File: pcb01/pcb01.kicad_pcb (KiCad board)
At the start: 2 copper layers, 7 parts, among them U1 W65C02SxP, U2 HM62256BLP, U3 27C512, U4 PAL20RS10, U5 74LS138, U6 74HCT574, U7 HM62256BLP

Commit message: more work on pcd layout
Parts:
- moved U5 100.3 mm to (13.3, 127.0)
- moved U4 92.6 mm to (41.3, 127.0)
- moved U6 86.0 mm to (108.0, 119.4), turned to -90 degrees
- moved U1 15.3 mm to (21.0, 61.0)
- moved U2 15.3 mm to (56.5, 76.2)
- moved U3 15.3 mm to (92.1, 76.2)
- moved U7 15.3 mm to (74.3, 76.2)
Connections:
- U3 pad 20: /CS_ROM -> /~{CS_ROM}
- U4 pad 16: /~{IO_SEL} -> /~{CS_RAM1}
- U4 pad 22: /~{CS_RAM1} -> /~{IO_SEL}
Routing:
- net /A14: track 28.3 -> 133.0 mm, vias 0 -> 5
- net /A12: track 42.6 -> 139.9 mm, vias 0 -> 5
- net /A13: track 58.4 -> 155.3 mm, vias 0 -> 5
- net GND: track 0.00 -> 96.4 mm
- net /A8: track 75.4 -> 154.3 mm, vias 0 -> 5
- net /A9: track 75.4 -> 154.3 mm, vias 0 -> 5
- net /A11: track 75.4 -> 151.8 mm, vias 0 -> 7
- net /~{QWE_RAM}: track 0.00 -> 70.8 mm, vias 0 -> 2
- net /SYS_CLK: track 0.00 -> 70.2 mm, vias 0 -> 1
- net /A10: track 94.3 -> 163.6 mm, vias 0 -> 7
- net /~{CS_ROM}: track 0.00 -> 65.7 mm, vias 0 -> 3
- net /R/~{W}: track 0.00 -> 62.0 mm, vias 0 -> 3
- net /A15: track 0.00 -> 61.1 mm, vias 0 -> 3
- net /~{CS_RAM0}: track 0.00 -> 50.4 mm, vias 0 -> 2
- net VCC: track 0.00 -> 46.7 mm
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- added copper zone on B.Cu, net GND
- added copper zone on F.Cu, net GND

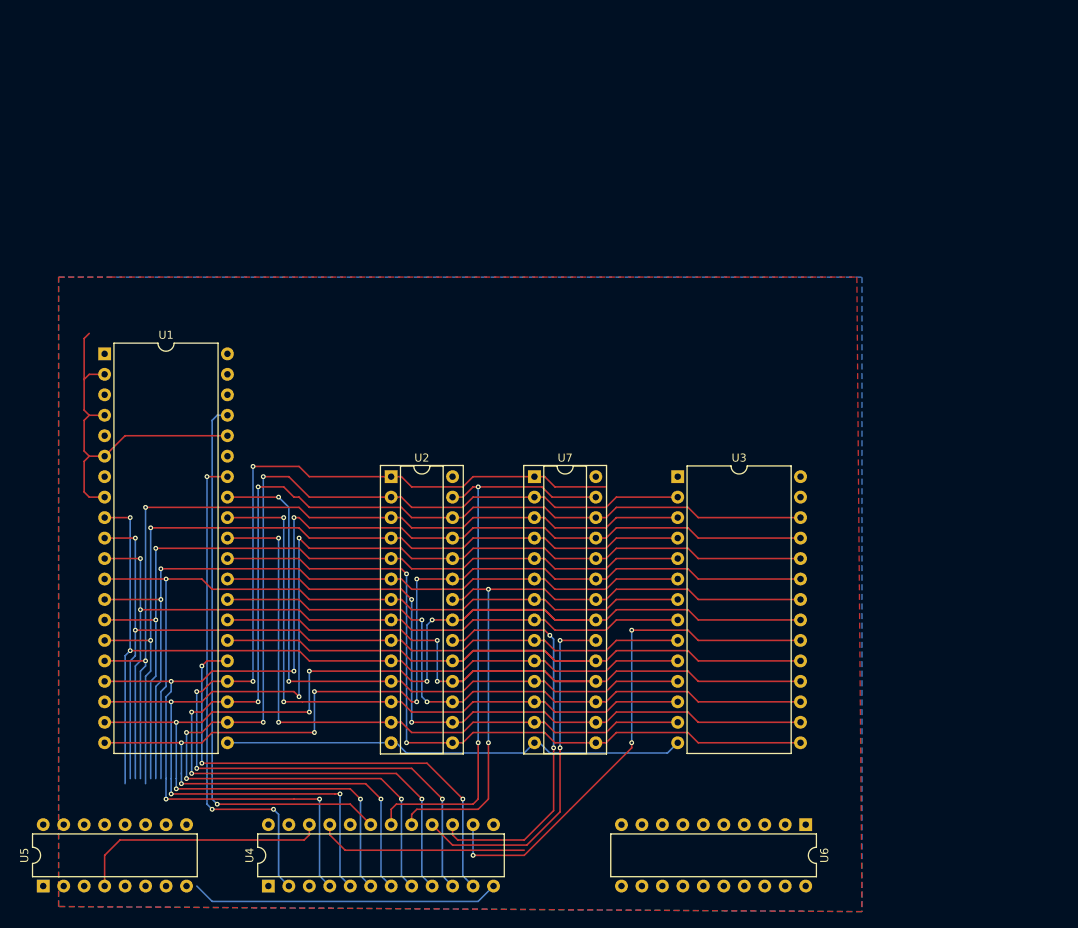
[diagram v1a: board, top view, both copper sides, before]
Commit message: wire in the R6552 uart
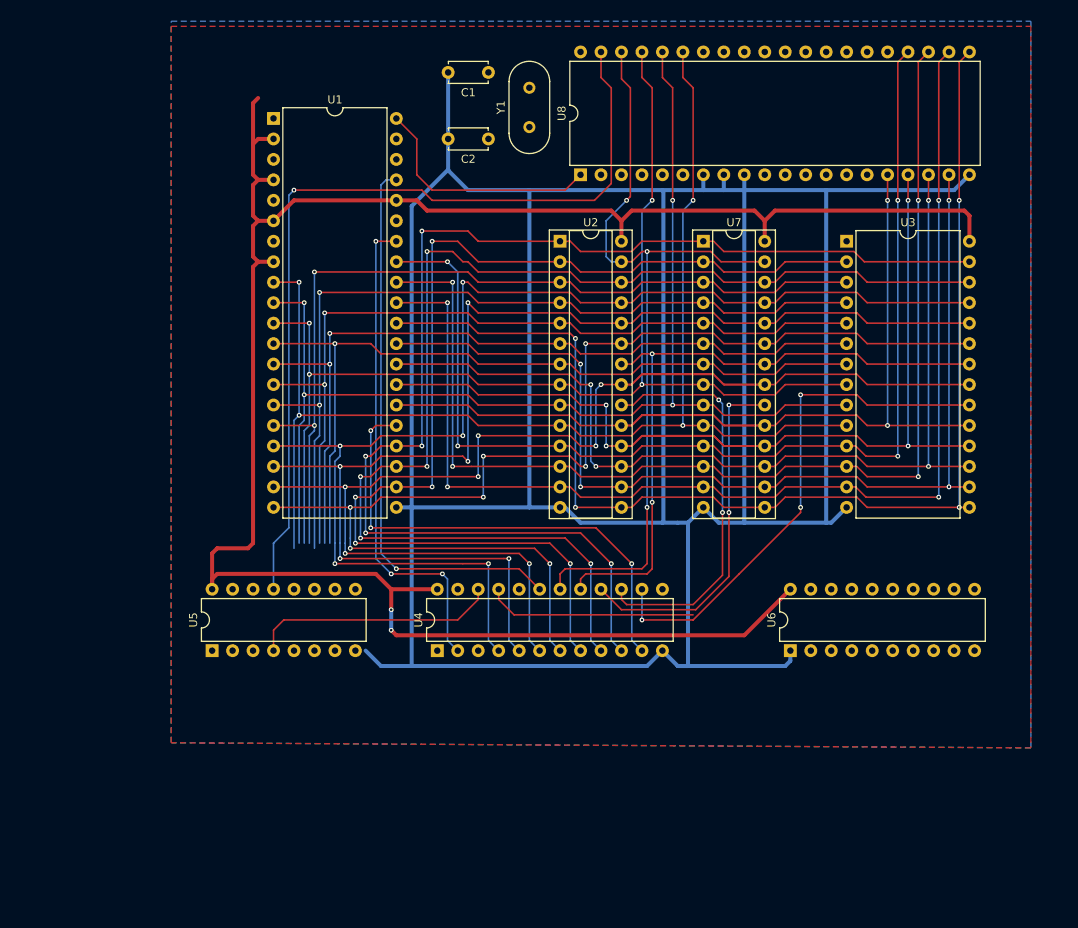
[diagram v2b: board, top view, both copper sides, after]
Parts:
- added C1: C, Capacitor_THT:C_Disc_D4.7mm_W2.5mm_P5.00mm, F.Cu at (68.6, 26.0)
- added C2: C, Capacitor_THT:C_Disc_D4.7mm_W2.5mm_P5.00mm, F.Cu at (68.6, 34.3)
- added U8: R565c52, Package_DIP:DIP-40_W15.24mm, F.Cu at (80.0, 38.7)
- added Y1: Crystal, Crystal:Crystal_HC49-4H_Vertical, F.Cu at (73.7, 32.8)
- moved U3 36.0 mm to (113.0, 47.0)
- moved U7 36.0 mm to (95.2, 47.0)
- moved U2 36.0 mm to (77.5, 47.0)
- moved U1 36.0 mm to (41.9, 31.8)
- moved U4 36.0 mm to (62.2, 97.8)
- moved U5 36.0 mm to (34.3, 97.8)
- moved U6 21.7 mm to (106.0, 97.8), turned to 90 degrees
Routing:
- net GND: track 96.4 -> 445.8 mm
- net VCC: track 46.7 -> 261.7 mm, vias 0 -> 2
- net /~{IOEN_02_UART}: track 0.00 -> 108.2 mm, vias 0 -> 1
- net /D2: track 80.8 -> 148.6 mm, vias 2 -> 4
- net /D1: track 80.8 -> 143.5 mm, vias 2 -> 4
- net /D0: track 80.1 -> 137.7 mm, vias 2 -> 4
- net /D3: track 95.0 -> 152.0 mm, vias 2 -> 4
- net /A0: track 107.0 -> 154.4 mm, vias 2 -> 4
- net /A1: track 103.9 -> 148.2 mm, vias 2 -> 4
- net /A2: track 101.3 -> 143.6 mm, vias 2 -> 4
- net /D4: track 89.5 -> 128.2 mm, vias 2 -> 4
- net /D5: track 84.1 -> 120.3 mm, vias 2 -> 4
- net /D6: track 98.2 -> 131.8 mm, vias 2 -> 4
- net /D7: track 93.1 -> 124.2 mm, vias 0 -> 2
- net /~{RES}: track 0.00 -> 29.9 mm
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- added copper zone on F.Cu, net VCC
- removed copper zone on F.Cu, net GND

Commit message: add reset circuit and filter caps
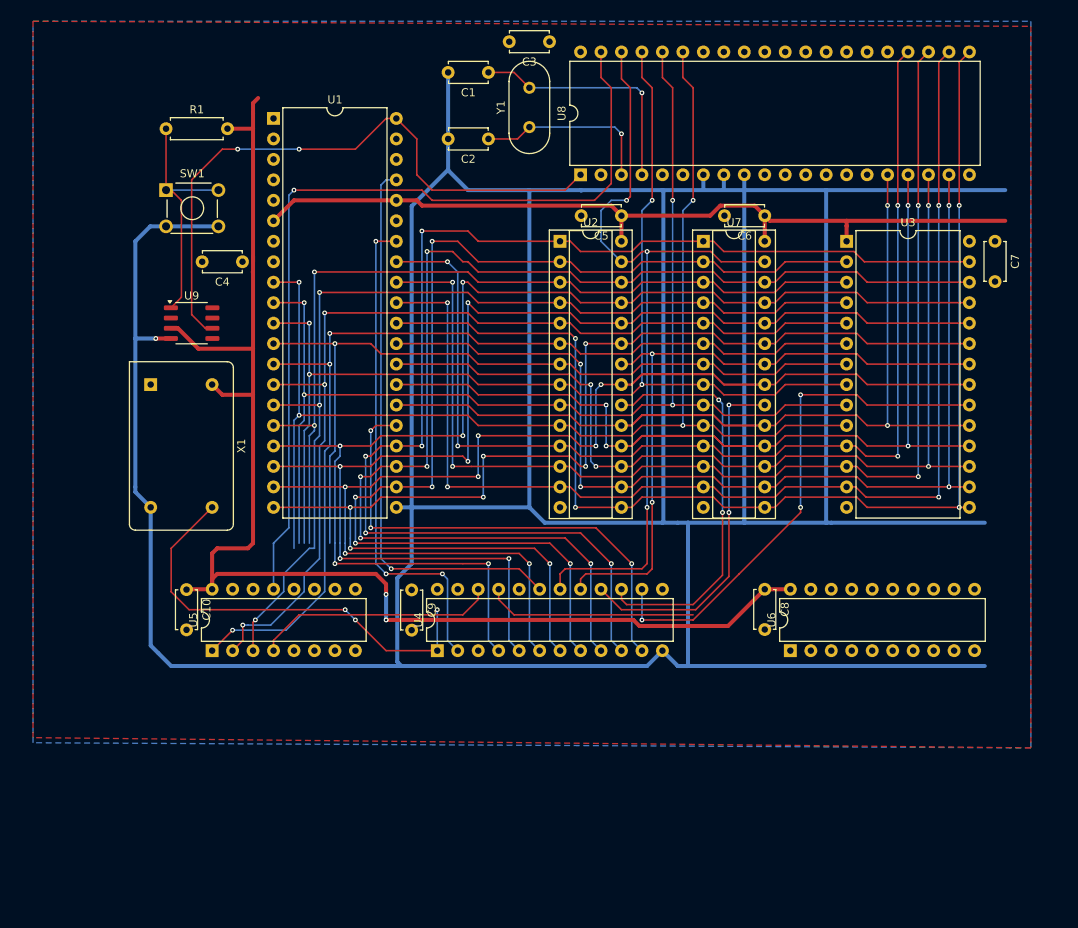
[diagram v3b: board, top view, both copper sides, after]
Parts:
- added C10: C, Capacitor_THT:C_Disc_D4.7mm_W2.5mm_P5.00mm, F.Cu at (31.1, 90.2)
- added C3: C, Capacitor_THT:C_Disc_D4.7mm_W2.5mm_P5.00mm, F.Cu at (76.2, 22.2)
- added C4: C, Capacitor_THT:C_Disc_D4.7mm_W2.5mm_P5.00mm, F.Cu at (38.1, 49.5)
- added C5: C, Capacitor_THT:C_Disc_D4.7mm_W2.5mm_P5.00mm, F.Cu at (85.1, 43.8)
- added C6: C, Capacitor_THT:C_Disc_D4.7mm_W2.5mm_P5.00mm, F.Cu at (102.9, 43.8)
- added C7: C, Capacitor_THT:C_Disc_D4.7mm_W2.5mm_P5.00mm, F.Cu at (131.4, 47.0)
- added C8: C, Capacitor_THT:C_Disc_D4.7mm_W2.5mm_P5.00mm, F.Cu at (102.9, 90.2)
- added C9: C, Capacitor_THT:C_Disc_D4.7mm_W2.5mm_P5.00mm, F.Cu at (59.1, 90.2)
- added R1: R, Resistor_THT:R_Axial_DIN0207_L6.3mm_D2.5mm_P7.62mm_Horizontal, F.Cu at (28.6, 33.0)
- added SW1: SW_Push, Button_Switch_THT:SW_TH_Tactile_Omron_B3F-10xx, F.Cu at (28.6, 40.6)
- added U9: ~, Package_SO:SO-8_3.9x4.9mm_P1.27mm, F.Cu at (31.8, 57.1)
- added X1: ACO-xxxMHz, Oscillator:Oscillator_DIP-14, F.Cu at (26.7, 64.8)
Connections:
- C1 pad 1: /UART_X1 -> /UART_X2
- C2 pad 1: /UART_X2 -> /UART_X1
- U1 pad 25: /A15 -> VCC
- U3 pad 1: /A15 -> VCC
- U4 pad 11: /A15 -> VCC
- Y1 pad 1: /UART_X2 -> /UART_X1
- Y1 pad 2: /UART_X1 -> /UART_X2
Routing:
- net GND: track 445.8 -> 581.9 mm, vias 0 -> 1
- net VCC: track 261.7 -> 333.8 mm, vias 2 -> 5
- net /A15: track 61.1 -> 0.00 mm, vias 3 -> 0
- net /CLOCK: track 0.00 -> 54.0 mm, vias 0 -> 3
- net /~{RES}: track 29.9 -> 78.5 mm, vias 0 -> 2
- net Net-(U9-~{PB_RST}): track 0.00 -> 30.4 mm
- net /UART_X2: track 0.00 -> 30.3 mm, vias 0 -> 1
- net /A4: track 100.0 -> 123.1 mm, vias 2 -> 3
- net /UART_X1: track 0.00 -> 22.5 mm, vias 0 -> 1
- net /A5: track 102.6 -> 122.4 mm, vias 2 -> 3
- net /A6: track 105.8 -> 122.0 mm, vias 2 -> 3
- net /~{QWE_RAM}: track 100.1 -> 101.0 mm
- net /~{IO_SEL}: track 30.8 -> 30.0 mm

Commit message: pcb layout should be finished...
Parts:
- added J1: DIN41612_02x32_AC, Connector_DIN:DIN41612_C_2x32_Male_Horizontal_THT, F.Cu at (123.8, 113.0)
- added J2: Conn_01x08_Socket, Connector_PinSocket_2.54mm:PinSocket_1x08_P2.54mm_Vertical, F.Cu at (108.6, 102.9)
- added J3: Conn_01x16_Socket, Connector_PinSocket_2.54mm:PinSocket_1x16_P2.54mm_Vertical, F.Cu at (49.5, 102.9)
- added J4: Conn_01x16_Socket, Connector_PinSocket_2.54mm:PinSocket_1x16_P2.54mm_Vertical, F.Cu at (135.9, 102.9)
- X1: footprint Oscillator:Oscillator_DIP-14 -> Package_DIP:DIP-14_W7.62mm
- turned X1 to 0 degrees
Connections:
- U1 pad 25: VCC -> /A15
- U4 pad 11: VCC -> /A15
- U5 pad 10: unconnected-(U5-O5-Pad10) -> /~{IOEN_05}
- U5 pad 11: unconnected-(U5-O4-Pad11) -> /~{IOEN_04}
- U5 pad 12: unconnected-(U5-O3-Pad12) -> /~{IOEN_03}
- U5 pad 7: unconnected-(U5-O7-Pad7) -> /~{IOEN_07}
- U5 pad 9: unconnected-(U5-O6-Pad9) -> /~{IOEN_06}
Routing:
- net /~{RES}: track 78.5 -> 222.8 mm, vias 2 -> 6
- net /~{IOEN_00_GPIO0}: track 0.00 -> 133.8 mm, vias 0 -> 3
- net /~{QWE_RAM}: track 101.0 -> 200.5 mm, vias 3 -> 7
- net /A0: track 154.4 -> 246.3 mm, vias 4 -> 6
- net /DISP_EN: track 26.2 -> 117.6 mm, vias 0 -> 2
- net /A15: track 0.00 -> 72.0 mm, vias 0 -> 3
- net /D0: track 137.7 -> 208.7 mm, vias 4 -> 6
- net /SYS_CLK: track 69.8 -> 138.2 mm, vias 1 -> 4
- net /D1: track 143.5 -> 204.6 mm, vias 4 -> 6
- net /A7: track 107.7 -> 164.4 mm, vias 2 -> 4
- net /D7: track 124.2 -> 173.1 mm, vias 2 -> 4
- net /D2: track 148.6 -> 197.2 mm, vias 4 -> 6
- net /~{QOE}: track 82.6 -> 128.9 mm, vias 2 -> 5
- net /D6: track 131.8 -> 177.7 mm, vias 4 -> 6
- net /A1: track 148.2 -> 192.6 mm
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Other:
- board outline added: 117.5 x 98.4 mm
- board text added: "JLCJLCJLCJLC"

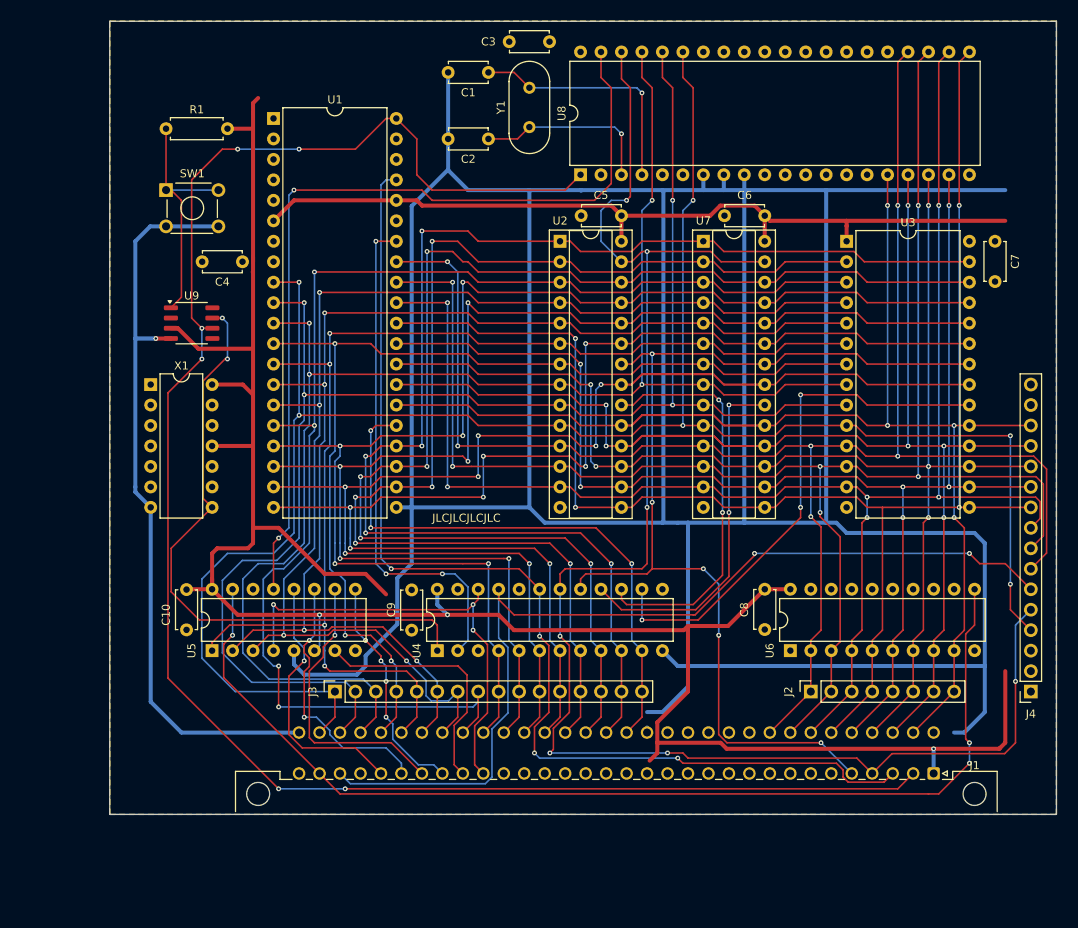
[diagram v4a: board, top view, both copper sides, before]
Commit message: fix some schematic bugs
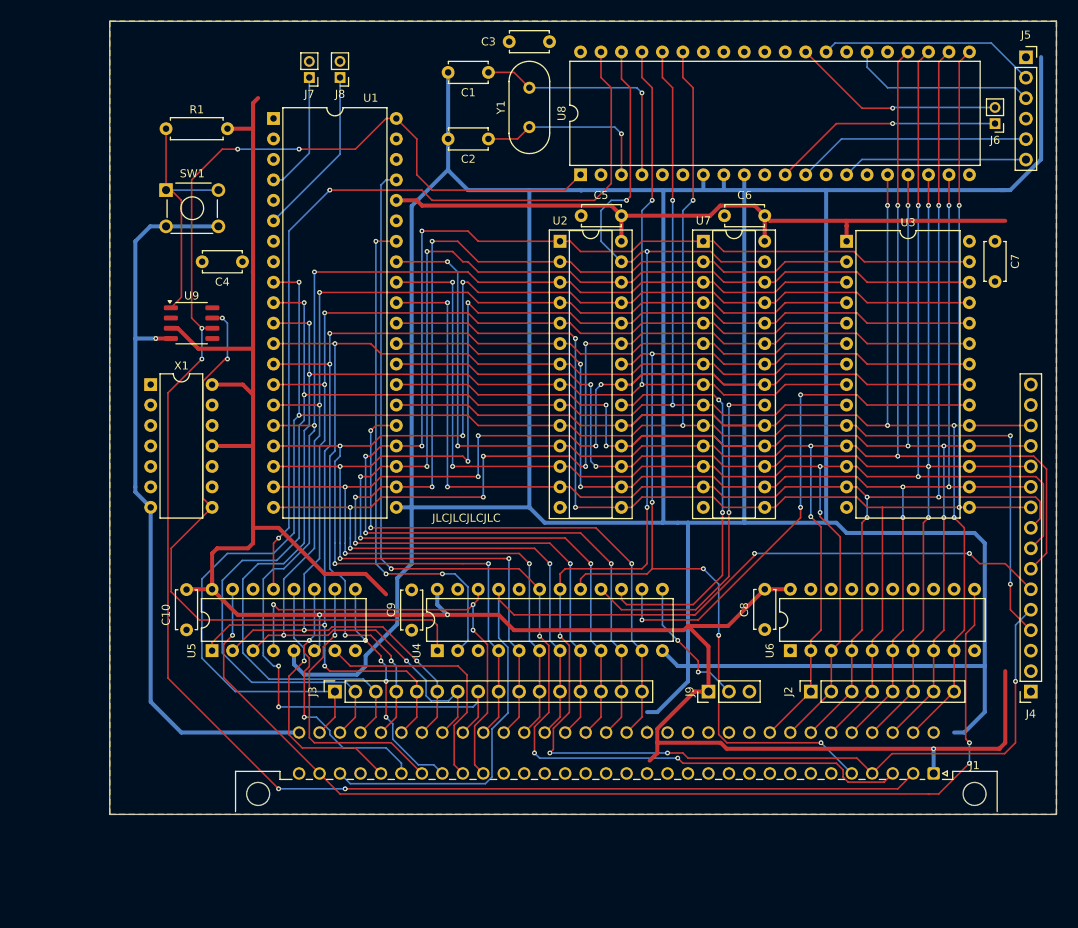
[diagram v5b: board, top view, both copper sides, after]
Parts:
- added J5: UART, Connector_PinSocket_2.54mm:PinSocket_1x06_P2.54mm_Vertical, F.Cu at (135.3, 24.2)
- added J6: UART_IRQ, Connector_PinHeader_2.00mm:PinHeader_1x02_P2.00mm_Vertical, F.Cu at (131.4, 32.4)
- added J7: Jmp_Irq, Connector_PinHeader_2.00mm:PinHeader_1x02_P2.00mm_Vertical, F.Cu at (46.4, 26.7)
- added J8: Jmp_NMI, Connector_PinHeader_2.00mm:PinHeader_1x02_P2.00mm_Vertical, F.Cu at (50.2, 26.7)
- added J9: Ram1 Enable, Connector_PinHeader_2.54mm:PinHeader_1x03_P2.54mm_Vertical, F.Cu at (95.9, 102.9)
- J2: value Conn_01x08_Socket -> Data Bus
- J3: value Conn_01x16_Socket -> Address Bus
- J4: value Conn_01x16_Socket -> Display
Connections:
- U1 pad 4: VCC -> /~{IRQ}
- U1 pad 6: VCC -> /~{NMI}
- U4 pad 13: GND -> Net-(J9-Pin_2)
- U8 pad 11: unconnected-(U8-~{IRQ2}-Pad11) -> Net-(J6-Pin_1)
- U8 pad 12: unconnected-(U8-RxD2-Pad12) -> /RX_D2
- U8 pad 14: unconnected-(U8-TxD2-Pad14) -> /TX_D2
- U8 pad 26: unconnected-(U8-TxD1-Pad26) -> /TX_D1
- U8 pad 28: unconnected-(U8-RxD1-Pad28) -> /RX_D1
- U8 pad 29: unconnected-(U8-~{IRQ1}-Pad29) -> Net-(J6-Pin_2)
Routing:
- net /RX_D2: track 0.00 -> 29.2 mm
- net Net-(J6-Pin_1): track 0.00 -> 28.7 mm, vias 0 -> 1
- net /RX_D1: track 0.00 -> 27.0 mm
- net Net-(J6-Pin_2): track 0.00 -> 26.4 mm, vias 0 -> 1
- net /TX_D1: track 0.00 -> 23.2 mm
- net /TX_D2: track 0.00 -> 23.0 mm
- net /~{NMI}: track 0.00 -> 21.2 mm
- net GND: track 593.0 -> 612.0 mm
- net Net-(J9-Pin_2): track 0.00 -> 16.9 mm, vias 0 -> 2
- net /~{IRQ}: track 0.00 -> 15.2 mm
- net VCC: track 377.5 -> 364.4 mm
- net /~{IOEN_02_UART}: track 108.2 -> 105.6 mm

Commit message: pcb refinement
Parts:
- added C11: C_Polarized, Capacitor_THT:CP_Radial_D8.0mm_P5.00mm, F.Cu at (38.7, 27.8)
- added C12: C_Polarized, Capacitor_THT:CP_Radial_D5.0mm_P2.50mm, F.Cu at (68.6, 44.5)
- added C13: C_Polarized, Capacitor_THT:CP_Radial_D5.0mm_P2.50mm, F.Cu at (98.4, 94.6)
- added J10: Conn_01x02_Socket, Connector_PinSocket_2.54mm:PinSocket_1x02_P2.54mm_Vertical, F.Cu at (31.1, 25.4)
- U1, U8: footprint Package_DIP:DIP-40_W15.24mm -> Package_DIP:DIP-40_W15.24mm_Socket
- U3: footprint Package_DIP:DIP-28_W15.24mm -> Package_DIP:DIP-28_W15.24mm_Socket
- U4: footprint Package_DIP:DIP-24_W7.62mm -> Package_DIP:DIP-24_W7.62mm_Socket
- U5: footprint Package_DIP:DIP-16_W7.62mm -> Package_DIP:DIP-16_W7.62mm_Socket
- U6: footprint Package_DIP:DIP-20_W7.62mm -> Package_DIP:DIP-20_W7.62mm_Socket
- U9: value ~ -> MAX1232
- X1: footprint Package_DIP:DIP-14_W7.62mm -> Package_DIP:DIP-14_W7.62mm_Socket
- moved C4 0.63 mm to (38.7, 49.5)
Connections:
- U4 pad 3: /IO_REQB_02_DISP -> /~{IOEN_01_DISP}
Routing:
- net GND: track 612.0 -> 685.4 mm, vias 1 -> 6
- net /~{IOEN_01_DISP}: track 0.00 -> 32.2 mm, vias 0 -> 1
- net /A10: track 174.6 -> 155.8 mm
- net /D7: track 173.1 -> 154.3 mm
- net /D6: track 177.7 -> 158.8 mm
- net VCC: track 364.4 -> 380.0 mm, vias 3 -> 1
- net /~{IOEN_05}: track 35.5 -> 31.8 mm
- net /~{IOEN_00_GPIO0}: track 133.8 -> 136.9 mm, vias 3 -> 4
- net /~{IOEN_06}: track 28.4 -> 31.5 mm, vias 4 -> 1
- net /A6: track 155.7 -> 153.0 mm
- net /~{QWE_RAM}: track 200.5 -> 197.9 mm, vias 7 -> 8
- net /CLOCK: track 77.3 -> 75.5 mm
- net /DISP_EN: track 117.6 -> 115.7 mm, vias 2 -> 4
- net /A1: track 192.6 -> 194.3 mm
- net /R/~{W}: track 63.6 -> 62.0 mm
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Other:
- board size 117.5 x 98.4 mm -> 118.1 x 98.4 mm
- board text added: "32K"
- board text added: "64K"
- board text added: "Address Bus"
- board text added: "Data Bus"
- board text added: "Display"
- board text added: "GND"
- board text added: "Irq"
- board text added: "NMI"
- board text added: "Ram"
- board text added: "Rx1"
- board text added: "Rx2"
- board text added: "Tx1"
- board text added: "Tx2"
- board text added: "Vcc"
